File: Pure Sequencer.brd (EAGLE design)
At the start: 119.9 x 100 mm, 132 parts, among them Q1 20MHz, T1 2N3904, T2 2N3904, U1 ATMEGA328P, U2 QUAD_OPAMP, U3 QUAD_OPAMP, U4 4051, U5 7805, U6 QUAD_OPAMP

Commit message: Sequencer 2.2
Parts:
- removed C11, C13, C15, C17, C19, C21, C23, C25, C8: *, rcl:C0805K
- removed C9: 47p, rcl:C0805K
- removed GLIDE1: rate, INSTRUO:Q-POT
- removed U$7: PB6149L-5, INSTRUO:PB6149L
- removed U1: ATMEGA328P, SparkFun-DigitalIC:TQFP32-08
- removed U2, U3, U6: QUAD_OPAMP, INSTRUO:QUAD_OPAMP
- removed U4: 4051, INSTRUO:N2222_ARRAY
- removed U5: 7805, INSTRUO:V-REG
- added D10, D3, D4, D5, D6, D7, D8, D9: 1N914, GMSN:DO-41
- added IC1: BA178M05FP, GMSN:TO252
- added IC2, IC3, IC4: TL074, GMSN:SO14
- added IC5: ATMEGA328P, GMSN:TQFP32-08
- added IC6: CD4051, GMSN:SOIC_16
- added R60: 200k, GMSN:R0805
- added R61: 100k, GMSN:R0805
- added RANGE: SWITCH_TOGGLE, GMSN:TOGGLE_SW
- added RATE: B100k, GMSN:POTENTIOMETER_9MM
- added SW1: (no value), GMSN:PB6149L
- added TR1: 100k, GMSN:TRIMMER_TH
- added U$1, U$2: (no value), gmsnLogo:GMSN!_LOGO
- C1, C2: value 22p -> 22pF; device rcl:C0805K -> GMSN:C0805
- C10, C12, C14, C16, C18, C20, C22, C24: value 47p -> 100pF; device rcl:C0805K -> GMSN:C0805
- C26, C4, C5: value 10u -> 10uF; device rcl:153CLV-0505 -> GMSN:153CLV-0505
- C27, C28, C29, C30, C31, C32, C33, C34, C35, C36: value 0.1u -> 100nF; device rcl:C0805K -> GMSN:C0805
- C3: device rcl:C0805K -> GMSN:C0805
- C6, C7: value 47p -> 47pF; device rcl:C0805K -> GMSN:C0805
- CLK_IN, CLOCK_OUT, CV_OUT, GATE1, GATE2, GATE3, GATE4, GATE5, GATE6, GATE7, GATE8, RESET: value (none) -> PJ301M-12; device INSTRUO:S_JACK -> GMSN:PJ301M-12
- D1, D2: value (none) -> STTH102A; device adafruit:SMADIODE -> GMSN:SMADIODE
- DIRSW: value (none) -> SWITCH_TOGGLE; device INSTRUO:TOGGLE_ON_OFF_ON -> GMSN:TOGGLE_SW
- FADER1, FADER2, FADER3, FADER4, FADER5, FADER6, FADER7, FADER8: value (none) -> 100k; device INSTRUO:LED_FADER -> GMSN:FADER_20MM_LED
- GLIDE: value B100K -> B100k; device INSTRUO:Q-POT -> GMSN:POTENTIOMETER_9MM
- ISP1: value AVRISP-6 -> HEADER2X3-6; device adafruit:AVRISP -> GMSN:AVRISP
- JP1: value M05X2SHD -> HEADER2X5SHD; device SparkFun-Connectors:2X5-SHROUDED -> GMSN:2X5-SHROUDED
- Q1: device adafruit:HC49UP -> GMSN:HC49UP
- R1: value 200R -> 0R; device rcl:R0805 -> GMSN:R0805
- R10, R15, R20, R25, R30, R35, R40, R45, R50, R56, R7: device rcl:R0805 -> GMSN:R0805
- R11, R12, R16, R17, R19, R21, R22, R24, R26, R27, R29, R31, R32, R34, R36, R37, R39, R41, R42, R44, R46, R47, R49, R51, R52, R54, R55, R58, R59, R6, R9: value 100K -> 100k; device rcl:R0805 -> GMSN:R0805
- R13, R14, R18, R23, R28, R33, R38, R43, R48, R53, R57: value 1K -> 1k; device rcl:R0805 -> GMSN:R0805
- R2: value 30K -> 34k; device rcl:R0805 -> GMSN:R0805
- R3: value 50K -> 56k; device rcl:R0805 -> GMSN:R0805
- R4: value 1K -> 0R; device rcl:R0805 -> GMSN:R0805
- R5, R8: value 10K -> 10k; device rcl:R0805 -> GMSN:R0805
- T1, T2: value 2N3904 -> MMBT3904; device INSTRUO:TRANSISTOR_SINGLE_N-TYPE -> GMSN:SOT23
- moved R14 36.8 mm to (111.2, 20.5), turned to 90 degrees
- moved R13 36.5 mm to (102.1, 20.5), turned to 180 degrees
- moved R12 34.8 mm to (97.5, 22.9), turned to 0 degrees
- moved R11 32.0 mm to (100.9, 24.0), turned to 90 degrees
- moved C7 31.4 mm to (103.4, 24.0), turned to 270 degrees
- moved DIRSW 30.0 mm to (31.0, 50.2)
- moved C31 29.7 mm to (115.9, 27.5), turned to 180 degrees
- moved R57 29.7 mm to (33.4, 45.7), turned to 90 degrees
- moved R3 27.9 mm to (117.0, 29.7), turned to 0 degrees
- moved R59 26.7 mm to (39.1, 53.5)
- moved R58 26.6 mm to (29.7, 54.7)
- moved C32 26.4 mm to (101.2, 27.9), turned to 180 degrees
- moved R2 25.0 mm to (117.0, 32.2), turned to 180 degrees
- moved C6 23.8 mm to (113.6, 31.0), turned to 90 degrees
- moved R4 20.6 mm to (115.3, 34.8), turned to 180 degrees
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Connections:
- removed net +5V: C26.+, C33.1, C34.1, C35.1, C36.1, FADER1.1, FADER2.1, FADER3.1, FADER4.1, FADER5.1, FADER6.1, FADER7.1, FADER8.1, GLIDE1.P$1, ISP1.2, R5.2, R57.1, R8.2, U$7.2, U$7.4, U1.18, U1.4, U1.6, U4.16, U5.3
- removed net MISO: ISP1.1, U1.16, U4.10
- removed net MOSI: ISP1.4, U1.15, U4.11
- removed net SCK: ISP1.3, U1.17, U4.9
- new net 5V: C26.+, C33.1, C34.1, C35.1, C36.1, FADER1.1, FADER2.1, FADER3.1, FADER4.1, FADER5.1, FADER6.1, FADER7.1, FADER8.1, IC1.2, IC5.18, IC5.4, IC5.6, IC6.16, ISP1.2, R5.2, R57.1, R8.2, RATE.P$1, SW1.3, SW1.4
- new net A: IC5.15, IC6.11, ISP1.4
- new net B: IC5.16, IC6.10, ISP1.1
- new net C: IC5.17, IC6.9, ISP1.3
- new net N$69: IC6.3, R60.2
- new net N$70: RANGE.2, TR1.2, TR1.3
- new net N$71: D6.C, GATE4.TIP
- new net N$72: D5.C, GATE3.TIP
- new net N$73: D4.C, GATE2.TIP
- new net N$74: D3.C, GATE1.TIP
- new net N$75: D10.C, GATE8.TIP
- new net N$76: D9.C, GATE7.TIP
- new net N$77: D8.C, GATE6.TIP
- new net N$78: D7.C, GATE5.TIP
- net +12V: now also IC1.1, IC2.4, IC3.4, IC4.4; no longer U2.VCC++, U3.VCC++, U5.1, U6.VCC++
- net -12V: now also IC2.11, IC3.11, IC4.11; no longer U2.VCC--, U3.VCC--, U6.VCC--
- net CLK_IN: now also IC5.32, T1.3; no longer T1.C, U1.32
- net CLK_OUT: now also IC2.10, IC5.14; no longer U1.14, U6.2+IN, U6.3+IN
- net G0: now also IC3.3, IC5.23; no longer U1.23, U2.1+IN
- net G1: now also IC3.5, IC5.24; no longer U1.24, U2.2+IN
- net G2: now also IC3.10, IC5.25; no longer U1.25, U2.3+IN
- net G3: now also IC3.12, IC5.26; no longer U1.26, U2.4+IN
- net G4: now also IC4.3, IC5.27; no longer U1.27, U3.1+IN
- net G5: now also IC4.5, IC5.28; no longer U1.28, U3.2+IN
- net G6: now also IC4.10, IC5.12; no longer U1.12, U3.3+IN
- net G7: now also IC4.12, IC5.13; no longer U1.13, U3.4+IN
- net GND: now also IC1.3, IC5.21, IC5.3, IC5.5, IC6.6, IC6.7, IC6.8, RANGE.3, RATE.P$3, T1.2, T2.2; no longer C11.2, C13.2, C15.2, C17.2, C19.2, C21.2, C23.2, C25.2, C8.2, GLIDE1.P$3, T1.E, T2.E, U1.21, U1.3, U1.5, U4.6, U4.7, U4.8, U5.4
- net N$1: now also IC5.7; no longer U1.7
- net N$11: now also IC6.1; no longer U4.1
- net N$12: now also IC6.12; no longer U4.12
- net N$13: now also IC6.15; no longer U4.15
- net N$14: now also IC6.14; no longer U4.14
- net N$15: now also IC6.13; no longer U4.13
- net N$16: now also IC2.3; no longer U6.1+IN
- net N$17: now also T1.1; no longer T1.B
- net N$18: now also IC2.5, R61.2; no longer CLK_IN.TIP, R6.2
- net N$19: now also IC2.2; no longer U6.1-IN
- net N$2: now also IC5.8; no longer U1.8
- net N$20: now also IC2.1; no longer U6.1OUT
- net N$22: now also T2.1; no longer T2.B
- net N$24: now also IC2.9; no longer C8.1, U6.3-IN
- net N$25: now also IC2.8; no longer U6.3OUT
- net N$26: now also CLK_IN.TIP, R6.2, R61.1; no longer CLOCK_OUT.TIP, R11.1, R13.1
- net N$27: now also IC2.6, IC2.7, R14.2; no longer C9.1, U6.2-IN
- net N$28: now also CLOCK_OUT.TIP, R14.1; no longer C9.2, R14.2, U6.2OUT
- net N$29: now also R11.1, R13.1; no longer R14.1
- net N$3: now also IC2.12, R60.1, TR1.1; no longer U4.3, U6.4+IN
- net N$30: now also IC5.22, RATE.P$2; no longer GLIDE1.P$2, U1.22
- net N$32: now also IC3.2; no longer C11.1, U2.1-IN
- net N$33: now also IC3.1; no longer U2.1OUT
- net N$34: now also D3.A; no longer GATE1.TIP
- net N$37: now also IC3.6; no longer C13.1, U2.2-IN
- net N$38: now also IC3.7; no longer U2.2OUT
- net N$39: now also D4.A; no longer GATE2.TIP
- net N$4: now also IC2.13, IC2.14; no longer U6.4-IN, U6.4OUT
- net N$40: now also IC3.9; no longer C15.1, U2.3-IN
- net N$41: now also IC3.8; no longer U2.3OUT
- net N$42: now also D5.A; no longer GATE3.TIP
- net N$44: now also IC3.13; no longer C17.1, U2.4-IN
- net N$45: now also IC3.14; no longer U2.4OUT
- net N$46: now also D6.A; no longer GATE4.TIP
- net N$48: now also IC4.2; no longer C19.1, U3.1-IN
- net N$49: now also IC4.1; no longer U3.1OUT
- net N$50: now also D7.A; no longer GATE5.TIP
- net N$52: now also IC4.6; no longer C21.1, U3.2-IN
- net N$53: now also IC4.7; no longer U3.2OUT
- net N$54: now also D8.A; no longer GATE6.TIP
- net N$56: now also IC4.9; no longer C23.1, U3.3-IN
- net N$57: now also IC4.8; no longer U3.3OUT
- net N$58: now also D9.A; no longer GATE7.TIP
- net N$6: now also IC6.4; no longer U4.4
- net N$60: now also IC4.13; no longer C25.1, U3.4-IN
- net N$61: now also IC4.14; no longer U3.4OUT
- net N$62: now also D10.A; no longer GATE8.TIP
- net N$63: now also IC5.2, SW1.1, SW1.2; no longer U$7.1, U$7.3, U1.2
- net N$64: now also IC5.9, SW1.A; no longer U$7.A, U1.9
- net N$65: now also SW1.K; no longer U$7.K
- net N$67: now also IC5.10; no longer U1.10
- net N$68: now also IC5.11; no longer U1.11
- net N$7: now also IC6.2; no longer U4.2
- net N$8: now also IC6.5; no longer U4.5
- net RESET: now also IC5.1, T2.3; no longer T2.C, U1.1
- net RST: now also IC5.29; no longer U1.29
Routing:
- net +5V: track 414.5 -> 0.00 mm, vias 7 -> 0
- net 5V: track 0.00 -> 374.8 mm, vias 0 -> 8
- net N$18: track 4.65 -> 111.7 mm, vias 0 -> 2
- net N$28: track 5.71 -> 80.7 mm, vias 0 -> 1
- net MOSI: track 58.1 -> 0.00 mm, vias 2 -> 0
- net A: track 0.00 -> 58.1 mm, vias 0 -> 2
- net SCK: track 47.1 -> 0.00 mm, vias 1 -> 0
- net C: track 0.00 -> 47.1 mm, vias 0 -> 1
- net MISO: track 46.6 -> 0.00 mm, vias 1 -> 0
- net B: track 0.00 -> 46.6 mm, vias 0 -> 1
- net N$26: track 44.1 -> 12.7 mm
- net N$29: track 71.0 -> 97.9 mm, vias 0 -> 1
- net N$67: track 46.7 -> 72.0 mm, vias 2 -> 4
- net CLK_OUT: track 53.7 -> 76.4 mm, vias 0 -> 2
- net N$68: track 45.2 -> 65.4 mm, vias 2 -> 4
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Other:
- board text added: "Pure Seq V2.2"
- board text added: "copyright GMSN Ltd 2016"

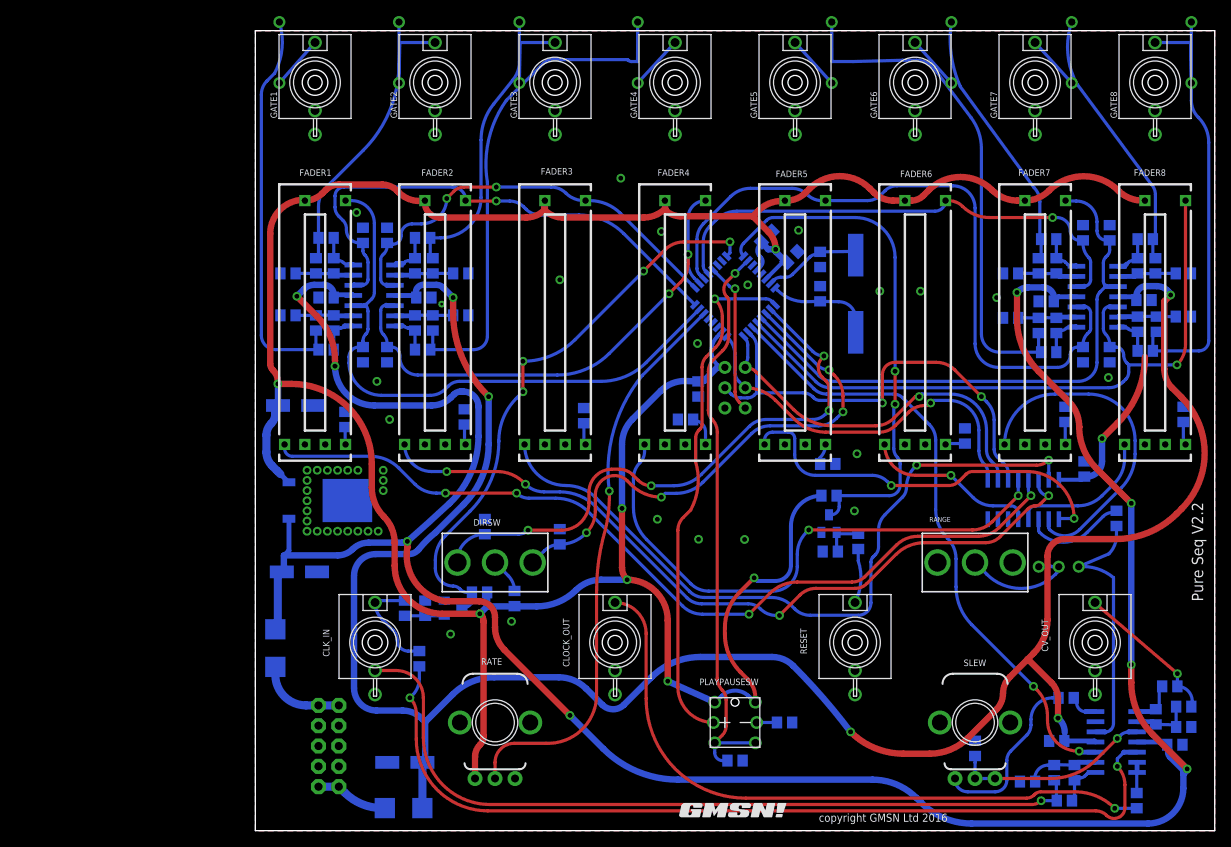
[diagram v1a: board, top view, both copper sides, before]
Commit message: Sequencer 2.3
Sequencer Updated to V2.3 20/4/21

Power Supply updated pull 5V from main case power supply, in line with low noise techniques.
Some resistor values reduced to 10k, in line with low noise techniques.
Traces rerouted.
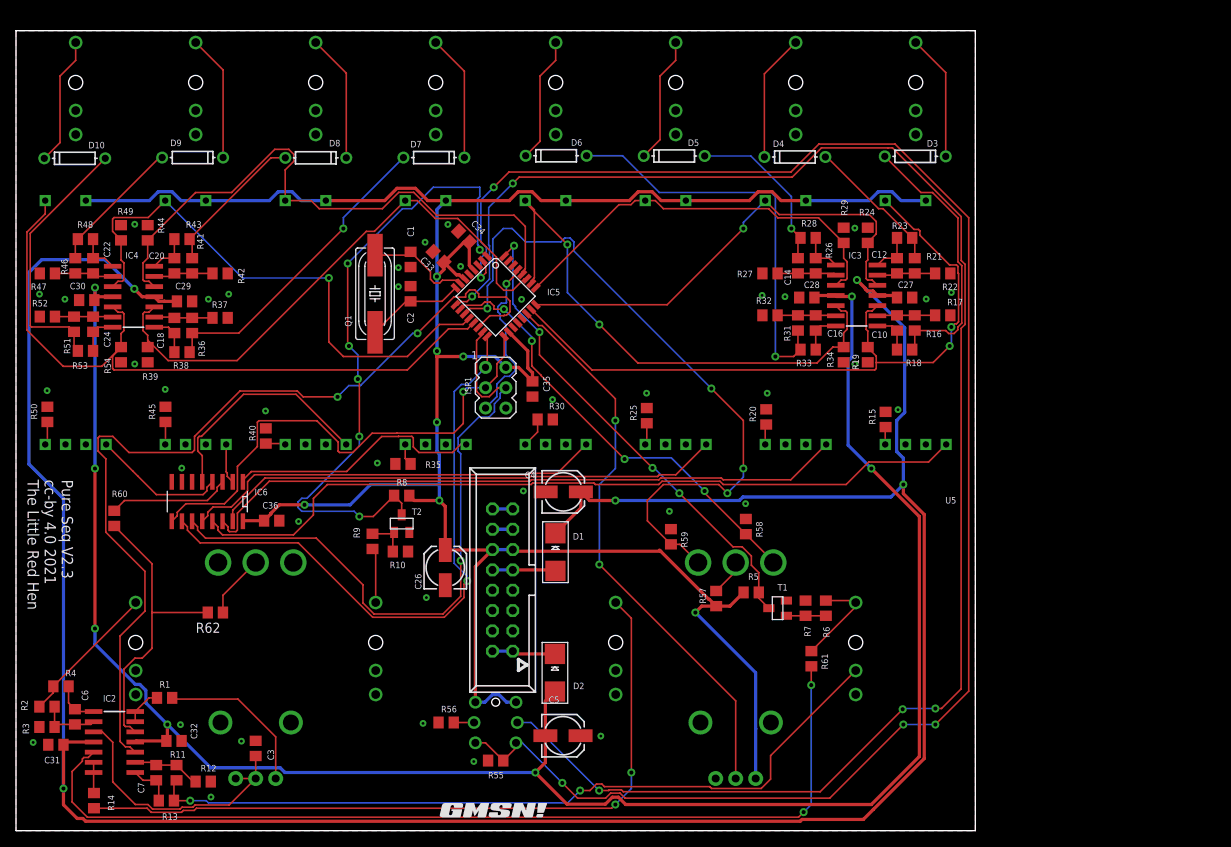
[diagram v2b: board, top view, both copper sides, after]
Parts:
- removed IC1: BA178M05FP, GMSN:TO252
- removed JP1: HEADER2X5SHD, GMSN:2X5-SHROUDED
- removed TR1: 100k, GMSN:TRIMMER_TH
- added JP2: HEADER2X8, GMSN:POWER_SHROUDED
- added R62: 50k, GMSN:R0805
- R1: value 0R -> 100R
- R16, R17, R21, R22, R26, R27, R31, R32, R36, R37, R41, R42, R46, R47, R51, R52: value 100k -> 10k
- R4: value 0R -> 1k
- moved R2 142.1 mm to (-25.0, 32.2), flipped to the top
- moved R3 142.1 mm to (-25.0, 29.7), flipped to the top
- moved R47 142.0 mm to (-25.0, 86.4), flipped to the top
- moved R50 142.0 mm to (-25.0, 68.8), flipped to the top
- moved R52 142.0 mm to (-25.0, 81.0), flipped to the top
- moved D10 140.2 mm to (-21.6, 100.8), flipped to the top, turned to 180 degrees
- moved C31 139.9 mm to (-23.9, 27.5), flipped to the top
- moved R4 138.6 mm to (-23.3, 34.8), flipped to the top
- moved R51 135.3 mm to (-21.7, 80.0), flipped to the top
- moved C6 135.1 mm to (-21.6, 31.0), flipped to the top
- moved R46 135.0 mm to (-21.5, 87.3), flipped to the top
- moved FADER8 134.9 mm to (-21.5, 80.2), flipped to the bottom
- moved GATE8 134.9 mm to (-21.5, 110.2), flipped to the bottom
- moved R48 132.5 mm to (-20.2, 90.7), flipped to the top
- moved R53 132.5 mm to (-20.2, 76.7), flipped to the top
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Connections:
- removed net N$10: D2.C, JP1.1, JP1.2
- new net GALL: IC5.19
- new net N$79: D2.C, JP2.1, JP2.2
- new net N$81: JP2.13, JP2.14
- new net N$82: JP2.15, JP2.16
- net +12V: no longer IC1.1
- net 5V: now also JP2.11, JP2.12; no longer IC1.2
- net GND: now also JP2.3, JP2.4, JP2.5, JP2.6, JP2.7, JP2.8; no longer IC1.3, JP1.3, JP1.4, JP1.5, JP1.6, JP1.7, JP1.8
- net N$3: now also R62.2; no longer TR1.1
- net N$70: now also R62.1; no longer TR1.2, TR1.3
- net N$9: now also JP2.10, JP2.9; no longer JP1.10, JP1.9
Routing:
- net N$63: track 71.4 -> 212.5 mm, vias 1 -> 5
- net N$64: track 64.3 -> 204.2 mm, vias 1 -> 5
- net 5V: track 374.8 -> 314.8 mm, vias 8 -> 7
- net +12V: track 290.0 -> 328.9 mm, vias 8 -> 5
- net CLK_OUT: track 76.4 -> 113.7 mm
- net N$7: track 40.0 -> 5.02 mm
- net B: track 46.6 -> 77.2 mm
- net N$13: track 89.9 -> 64.0 mm, vias 2 -> 0
- net N$50: track 63.8 -> 38.8 mm, vias 0 -> 1
- net A: track 58.1 -> 82.5 mm, vias 2 -> 1
- net N$68: track 65.4 -> 87.2 mm
- net N$62: track 50.4 -> 33.2 mm
- net N$12: track 69.7 -> 52.9 mm, vias 2 -> 0
- net RESET: track 64.2 -> 80.8 mm, vias 2 -> 6
- net C: track 47.1 -> 63.6 mm
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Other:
- board text added: "Pure Seq V2.3 cc-by 4.0 2021 The Little Red Hen"
- board text removed: "-12V"
- board text removed: "Pure Seq V2.2"
- board text removed: "copyright GMSN Ltd 2016"

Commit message: Reinstall
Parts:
- FADER1, FADER2, FADER3, FADER4, FADER5, FADER6, FADER7, FADER8: value 100k -> 50k
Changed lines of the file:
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@@
 <drawing>
 <settings>
-<setting alwaysvectorfont="yes"/>
+<setting alwaysvectorfont="no"/>
 <setting keepoldvectorfont="yes"/>
 <setting verticaltext="up"/>
@@
 <attribute name="VALUE" x="36.16025" y="39.01375" size="0.4064" layer="27" font="vector" rot="R270"/>
 </element>
-<element name="FADER1" library="GMSN" package="FADER_20MM_LED" value="100k" x="83.54" y="80.25" smashed="yes" rot="MR0">
+<element name="FADER1" library="GMSN" package="FADER_20MM_LED" value="50k" x="83.54" y="80.25" smashed="yes" rot="MR0">
 <attribute name="SORT" value="7" x="83.54" y="80.25" size="1.778" layer="28" rot="MR0" display="off"/>
 </element>
-<element name="FADER2" library="GMSN" package="FADER_20MM_LED" value="100k" x="68.54" y="80.25" smashed="yes" rot="MR0">
+<element name="FADER2" library="GMSN" package="FADER_20MM_LED" value="50k" x="68.54" y="80.25" smashed="yes" rot="MR0">
 <attribute name="SORT" value="7" x="68.54" y="80.25" size="1.778" layer="28" rot="MR0" display="off"/>
 </element>
-<element name="FADER3" library="GMSN" package="FADER_20MM_LED" value="100k" x="53.54" y="80.25" smashed="yes" rot="MR0">
+<element name="FADER3" library="GMSN" package="FADER_20MM_LED" value="50k" x="53.54" y="80.25" smashed="yes" rot="MR0">
 <attribute name="SORT" value="7" x="53.54" y="80.25" size="1.778" layer="28" rot="MR0" display="off"/>
 </element>
-<element name="FADER4" library="GMSN" package="FADER_20MM_LED" value="100k" x="38.54" y="80.25" smashed="yes" rot="MR0">
+<element name="FADER4" library="GMSN" package="FADER_20MM_LED" value="50k" x="38.54" y="80.25" smashed="yes" rot="MR0">
 <attribute name="SORT" value="7" x="38.54" y="80.25" size="1.778" layer="28" rot="MR0" display="off"/>
 </element>
-<element name="FADER5" library="GMSN" package="FADER_20MM_LED" value="100k" x="23.54" y="80.25" smashed="yes" rot="MR0">
+<element name="FADER5" library="GMSN" package="FADER_20MM_LED" value="50k" x="23.54" y="80.25" smashed="yes" rot="MR0">
 <attribute name="SORT" value="7" x="23.54" y="80.25" size="1.778" layer="28" rot="MR0" display="off"/>
 </element>
-<element name="FADER6" library="GMSN" package="FADER_20MM_LED" value="100k" x="8.54" y="80.25" smashed="yes" rot="MR0">
+<element name="FADER6" library="GMSN" package="FADER_20MM_LED" value="50k" x="8.54" y="80.25" smashed="yes" rot="MR0">
 <attribute name="SORT" value="7" x="8.54" y="80.25" size="1.778" layer="28" rot="MR0" display="off"/>
 </element>
-<element name="FADER7" library="GMSN" package="FADER_20MM_LED" value="100k" x="-6.46" y="80.25" smashed="yes" rot="MR0">
+<element name="FADER7" library="GMSN" package="FADER_20MM_LED" value="50k" x="-6.46" y="80.25" smashed="yes" rot="MR0">
 <attribute name="SORT" value="7" x="-6.46" y="80.25" size="1.778" layer="28" rot="MR0" display="off"/>
 </element>
-<element name="FADER8" library="GMSN" package="FADER_20MM_LED" value="100k" x="-21.46" y="80.25" smashed="yes" rot="MR0">
+<element name="FADER8" library="GMSN" package="FADER_20MM_LED" value="50k" x="-21.46" y="80.25" smashed="yes" rot="MR0">
 <attribute name="SORT" value="7" x="-21.46" y="80.25" size="1.778" layer="28" rot="MR0" display="off"/>
 </element>
